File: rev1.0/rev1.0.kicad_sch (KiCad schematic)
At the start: 17 parts, among them J1 Conn_01x06_Pin, J3 Conn_01x06_Socket, J4 Conn_01x06_Socket, SW1 SW_DIP_x05, U1 74HC595, U2 74HC595, U3 74HC165

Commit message: oop, forgot the PCB changes
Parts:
- added C1, C2, C3: 100nf, Capacitor_SMD:C_0603_1608Metric, symbol Device:C_Small
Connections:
- net 5V is gone; now on net VCC: J1.5 (Pin_5), J3.5 (Pin_5), J4.5 (Pin_5)
- net Clock: now also U1.11 (SRCLK), U2.11 (SRCLK)
- net GND: now also U1.13 (~{OE}), U2.13 (~{OE}), C1.1, C2.1, C3.1
- net Shift/load: now also U1.12 (RCLK), U2.12 (RCLK)
- net VCC: now also U1.10 (~{SRCLR}), U2.10 (~{SRCLR}), C1.2, C2.2, C3.2

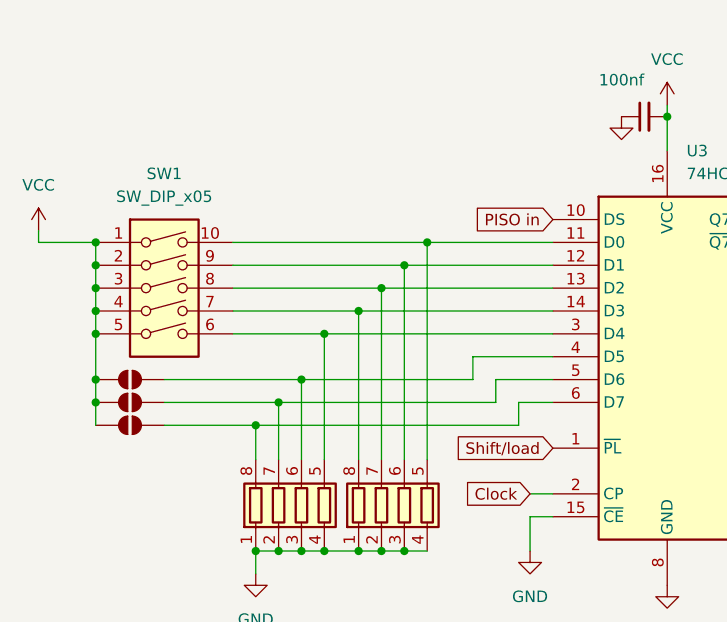
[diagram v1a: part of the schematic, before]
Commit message: Gikk over til 4-lags for å få det mye mindre.
Byttet også over til en full 8pin DIP-swith, og mindre pakke en jeg hadde først
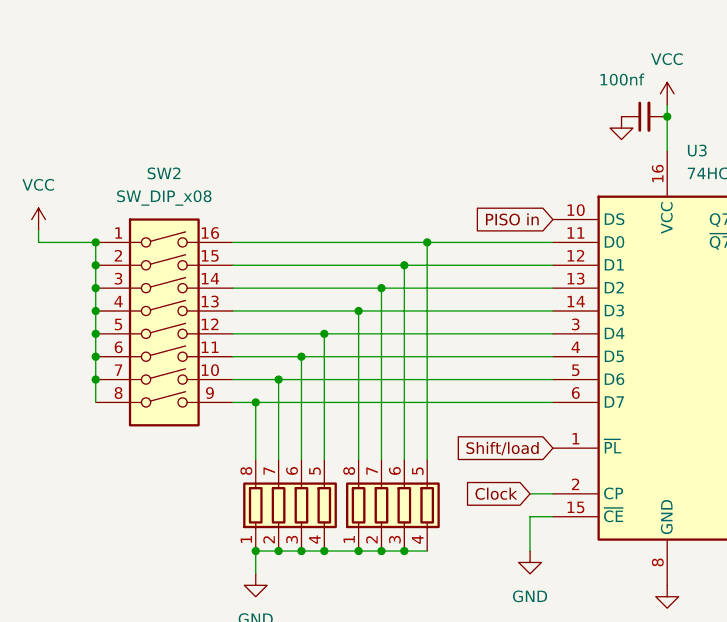
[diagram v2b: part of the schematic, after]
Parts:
- removed JP1, JP2, JP3: SolderJumper_2_Open, Jumper:SolderJumper-2_P1.3mm_Open_TrianglePad1.0x1.5mm, symbol Jumper:SolderJumper_2_Open
- removed SW1: SW_DIP_x05, Button_Switch_SMD:SW_DIP_SPSTx05_Slide_6.7x14.26mm_W8.61mm_P2.54mm_LowProfile, symbol Switch:SW_DIP_x05
- added SW2: SW_DIP_x08, Package_SO:SOIC-16_3.9x9.9mm_P1.27mm, symbol Switch:SW_DIP_x08
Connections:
- net VCC: now also SW2.1, SW2.2, SW2.3, SW2.4, SW2.5, SW2.6, SW2.7, SW2.8
- net at RN2.5 (R4.2), U3.11 (D0): now also SW2.16
- net at RN2.6 (R3.2), U3.12 (D1): now also SW2.15
- net at RN2.7 (R2.2), U3.13 (D2): now also SW2.14
- net at RN2.8 (R1.2), U3.14 (D3): now also SW2.13
- net at RN1.5 (R4.2), U3.3 (D4): now also SW2.12
- net at RN1.6 (R3.2), U3.4 (D5): now also SW2.11
- net at RN1.7 (R2.2), U3.5 (D6): now also SW2.10
- net at RN1.8 (R1.2), U3.6 (D7): now also SW2.9

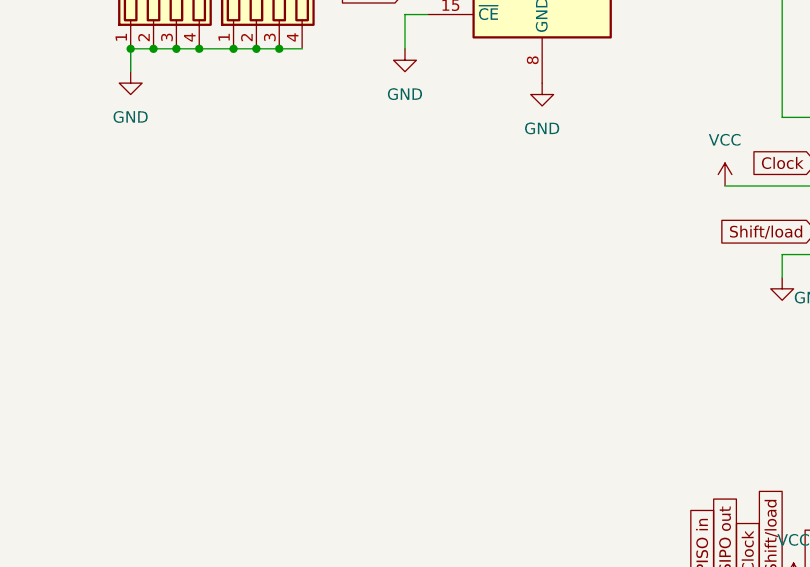
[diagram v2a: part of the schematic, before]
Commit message: Started coding.
Reading and writing to registers implemented.
The circuit is now on rev 1.1, but there were some mistakes on this one to, hehe.
The dip-switch is NOT the same size as a 16p soic, a little wider (bodgedd by bending pins under on one side (the one thats just all vcc anyways, as it can be bridged if you're struggeling with the jank solder)).
The socket also has some mechanical solder points on the ends, that wasnt on my footprint. They are also thinner and longer than thought. The mechanical solder on one side could short some pins on the 165, but i simply put a piece of kapton tape acrross the pins. Circuit works otherwise. Perhaps a little hot. Maybe not ideal to drive LEDs directly from 595's, but they can probably handle it
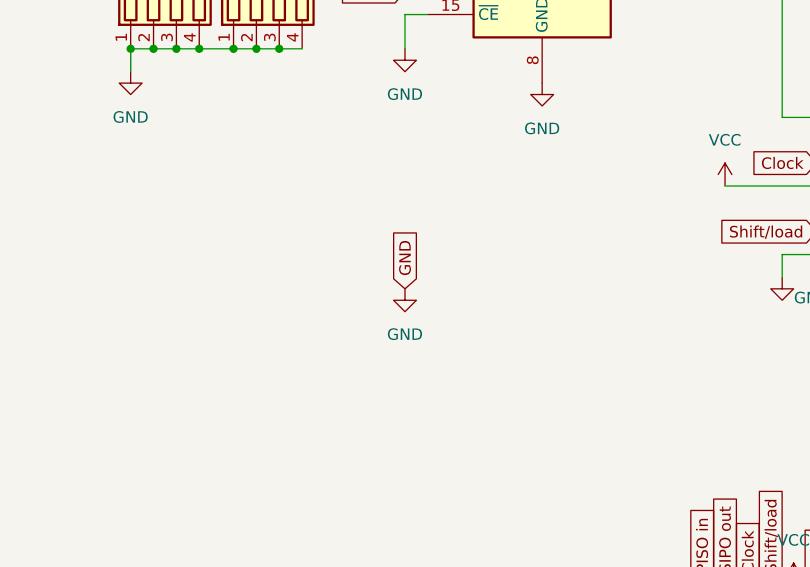
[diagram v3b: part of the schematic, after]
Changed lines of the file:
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@@
+		)
+	)
+	(global_label "GND"
+		(shape input)
+		(at 97.79 116.84 90)
+		(fields_autoplaced yes)
+		(effects
+			(font
+				(size 1.27 1.27)
+			)
+			(justify left)
+		)
+		(property "Intersheetrefs" "${INTERSHEET_REFS}"
+			(at 97.79 109.9843 90)
+			(effects
+				(font
+					(size 1.27 1.27)
+				)
+				(justify left)
+				(hide yes)
+			)
 		)
 	)
@@
 					(unit 1)
 				)
+			)
+		)
+	)
+	(symbol
+		(lib_id "power:GND")
+		(at 97.79 116.84 0)
+		(unit 1)
+		(exclude_from_sim no)
+		(in_bom yes)
+		(on_board yes)
+		(dnp no)
+		(fields_autoplaced yes)
+		(property "Reference" "#PWR07"
+			(at 97.79 123.19 0)
+			(effects
+				(font
+					(size 1.27 1.27)
+				)
+				(hide yes)
+			)
+		)
+		(property "Value" "GND"
+			(at 97.79 121.92 0)
+			(effects
+				(font
+					(size 1.27 1.27)
+				)
+			)
+		)
+		(property "Footprint" ""
+			(at 97.79 116.84 0)
+			(effects
+				(font
+					(size 1.27 1.27)
+				)
+				(hide yes)
+			)
+		)
+		(property "Datasheet" ""
+			(at 97.79 116.84 0)
+			(effects
+				(font
+					(size 1.27 1.27)
+				)
+				(hide yes)
+			)
+		)
+		(property "Description" "Power symbol creates a global label with name \"GND\" , ground"
+			(at 97.79 116.84 0)
+			(effects
+				(font
+					(size 1.27 1.27)
+				)
+				(hide yes)
+			)
+		)
+		(pin "1"
+		)
+		(instances
+			(project "rev1.0"
+				(path "/8fe827c4-7a1d-475b-9b07-36920366e461"
+					(reference "#PWR07")
+					(unit 1)
+				)
